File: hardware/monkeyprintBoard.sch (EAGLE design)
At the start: 46 parts, among them Q1 BSS123

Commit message: Updated eagle files.
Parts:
- removed GPIO: (no value), connectors:X05X2D
- removed H1, H2, H3, H4: MOUNT-HOLE3.0, holes:MOUNT-HOLE3.0
- removed U$2, U$3: POLOLU8825, pololu8825:POLOLU8825
- added ARDUINO_PRO_MICRO: ARDUINOPROMICRO, arduinoProMicro:ARDUINOPROMICRO
- added C7: 100n, rcl:C-EUC0603
- added POLOLU_DRV8825_BUILD, POLOLU_DRV8825_TILT: POLOLU8825, pololu8825:POLOLU8825
- added R15: 220R, rcl:R-EU_R0603
- added R17: 10k, rcl:R-EU_R0603
- added R19: 0R, rcl:R-EU_R0603
- added X3: (no value), connectors:X02
- U$1: value ARDUINOPROMICRO -> MONKEYPRINTPICONNECTOR; device arduinoProMicro:ARDUINOPROMICRO -> monkeyprintPiConnector:MONKEYPRINTPICONNECTOR
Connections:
- new net N$49: R17.1, R19.2, U$6.6
- new net N$50: ARDUINO_PRO_MICRO.(MOSI)PB2, C7.1, R19.1
- net GND: now also ARDUINO_PRO_MICRO.GND1, ARDUINO_PRO_MICRO.GND2, ARDUINO_PRO_MICRO.GND3, C7.2, POLOLU_DRV8825_BUILD.GND1, POLOLU_DRV8825_BUILD.GND2, POLOLU_DRV8825_TILT.GND1, POLOLU_DRV8825_TILT.GND2, X3.2; no longer GPIOA.9, GPIOB.6, U$1.GND3, U$2.GND1, U$2.GND2, U$3.GND1, U$3.GND2
- net N$1: now also ARDUINO_PRO_MICRO.PD4, POLOLU_DRV8825_BUILD.DIR; no longer U$1.PD4, U$2.DIR
- net N$12: now also ARDUINO_PRO_MICRO.PD1(INT1/SDA); no longer U$1.PD1(INT1/SDA)
- net N$13: now also ARDUINO_PRO_MICRO.PD0(INT0/SCL/OC0B); no longer U$1.PD0(INT0/SCL/OC0B)
- net N$15: now also POLOLU_DRV8825_BUILD.2A; no longer U$2.2A
- net N$16: now also POLOLU_DRV8825_BUILD.1A; no longer U$2.1A
- net N$17: now also POLOLU_DRV8825_BUILD.1B; no longer U$2.1B
- net N$18: now also POLOLU_DRV8825_TILT.2A; no longer U$3.2A
- net N$19: now also POLOLU_DRV8825_TILT.1A; no longer U$3.1A
- net N$2: now also ARDUINO_PRO_MICRO.PC6(OC3A), POLOLU_DRV8825_BUILD.STEP; no longer U$1.PC6(OC3A), U$2.STEP
- net N$20: now also POLOLU_DRV8825_TILT.1B; no longer U$3.1B
- net N$21: now also POLOLU_DRV8825_TILT.2B; no longer U$3.2B
- net N$22: now also POLOLU_DRV8825_TILT.M0; no longer U$3.M0
- net N$23: now also POLOLU_DRV8825_TILT.M1; no longer U$3.M1
- net N$24: now also POLOLU_DRV8825_TILT.M2; no longer U$3.M2
- net N$25: now also ARDUINO_PRO_MICRO.PE6(INT6); no longer U$1.PE6(INT6)
- net N$26: now also ARDUINO_PRO_MICRO.PD3(INT3/TXD), U$1.RXD; no longer GPIOB.10, U$1.PD3(INT3/TXD)
- net N$27: now also ARDUINO_PRO_MICRO.(OC1B)PB6; no longer U$1.(OC1B)PB6
- net N$28: now also ARDUINO_PRO_MICRO.RESET; no longer U$1.RESET
- net N$29: now also ARDUINO_PRO_MICRO.(SCK)PB1, U$7.4; no longer U$1.(SCK)PB1, U$7.1
- net N$31: now also X3.1; no longer U$7.4
- net N$32: now also ARDUINO_PRO_MICRO.PF5; no longer U$1.PF5
- net N$33: now also ARDUINO_PRO_MICRO.VCC; no longer U$1.VCC
- net N$34: now also ARDUINO_PRO_MICRO.PF4; no longer U$1.PF4
- net N$37: now also ARDUINO_PRO_MICRO.PD2(INT2/RXD), U$1.TXD; no longer GPIOB.8, U$1.PD2(INT2/RXD)
- net N$38: now also ARDUINO_PRO_MICRO.(MISO/LED)PB3, U$7.6; no longer U$1.(MISO/LED)PB3, U$7.3
- net N$39: now also ARDUINO_PRO_MICRO.PD7(OC4D), U$7.1; no longer U$1.PD7(OC4D), U$6.4
- net N$4: now also ARDUINO_PRO_MICRO.PB5(OC1A), POLOLU_DRV8825_TILT.STEP; no longer U$1.PB5(OC1A), U$3.STEP
- net N$41: now also R15.1, U$6.4; no longer U$1.(MOSI)PB2, U$7.6
- net N$42: now also POLOLU_DRV8825_BUILD.2B; no longer U$2.2B
- net N$43: now also POLOLU_DRV8825_BUILD.VMOTOR; no longer U$2.VMOTOR
- net N$44: now also POLOLU_DRV8825_BUILD.M0; no longer U$2.M0
- net N$45: now also POLOLU_DRV8825_BUILD.M1; no longer U$2.M1
- net N$46: now also POLOLU_DRV8825_BUILD.M2; no longer U$2.M2
- net N$5: now also ARDUINO_PRO_MICRO.PF6, POLOLU_DRV8825_BUILD.RESET, POLOLU_DRV8825_BUILD.SLEEP; no longer U$1.PF6, U$2.RESET, U$2.SLEEP
- net N$6: now also ARDUINO_PRO_MICRO.PB4, POLOLU_DRV8825_TILT.DIR; no longer U$1.PB4, U$3.DIR
- net N$8: now also ARDUINO_PRO_MICRO.PF7, POLOLU_DRV8825_TILT.RESET, POLOLU_DRV8825_TILT.SLEEP; no longer U$1.PF7, U$3.RESET, U$3.SLEEP
- net V+: now also POLOLU_DRV8825_TILT.VMOTOR; no longer U$3.VMOTOR
- net VCC: now also R15.2, R17.2, U$1.VCC1, U$1.VCC2, U$7.3; no longer GPIOB.2, GPIOB.4, U$6.6
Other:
- note added: "End stop tilt 2"
- note added: "LM2596"
- note added: "Raspberry Pi GPIO connector"
- note removed: "Camera trigger"
- moved on the sheet: C1, C2, C3, C4, C5, C6, D1, FAN, J1, J2, J3, J4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

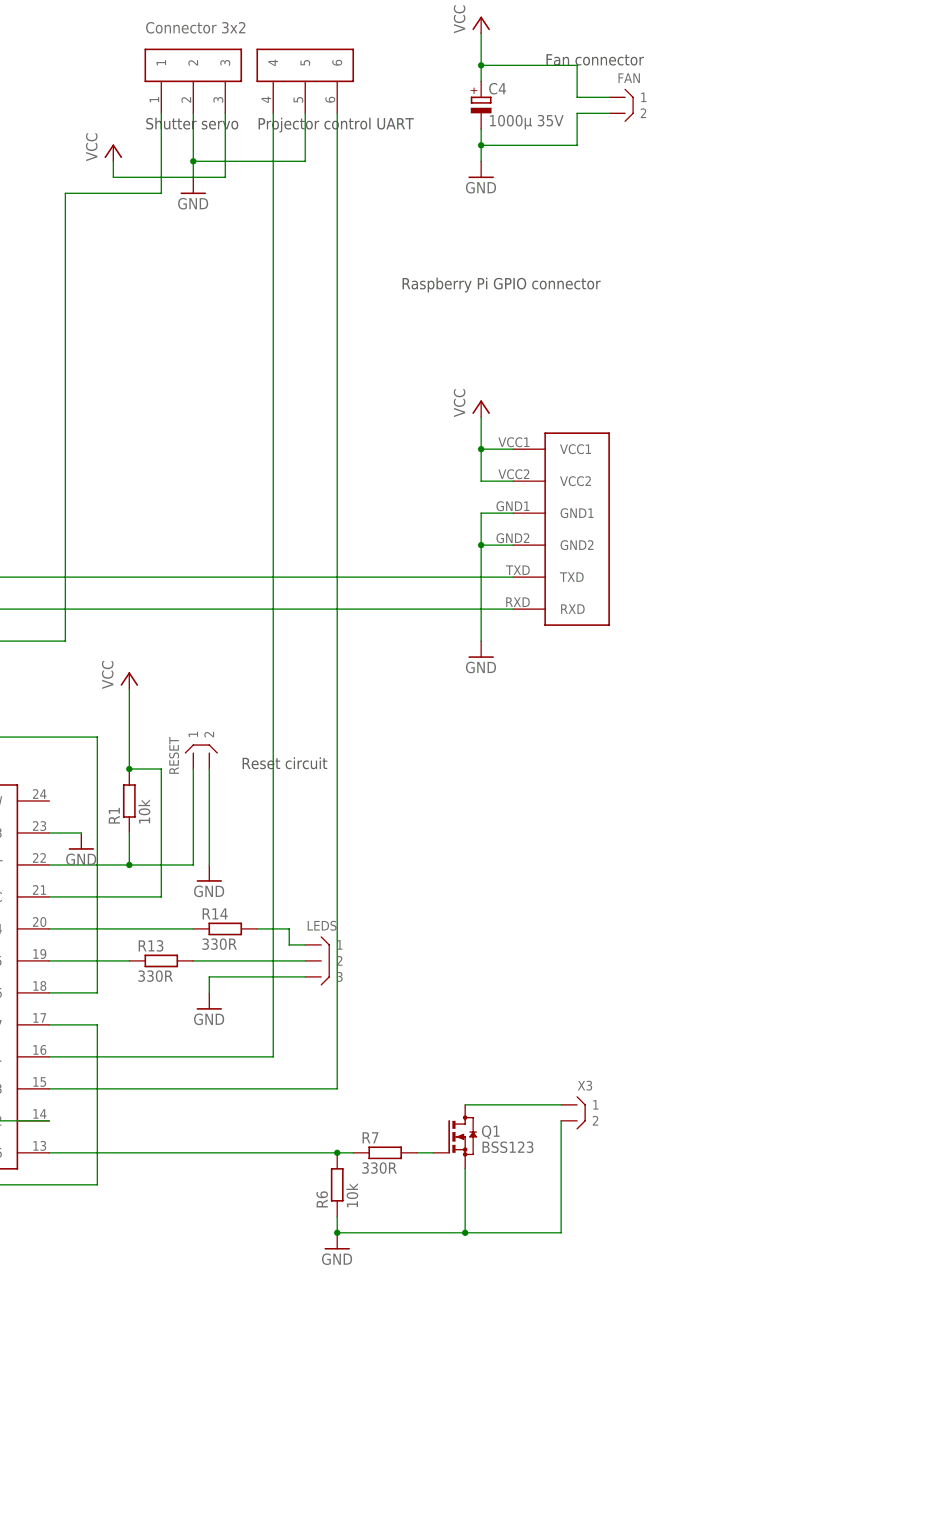
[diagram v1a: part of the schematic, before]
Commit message: Published board version 0.92. Fixed shutter servo pinout, swapped gnd and vcc to accomodate most common servo connector pinout.
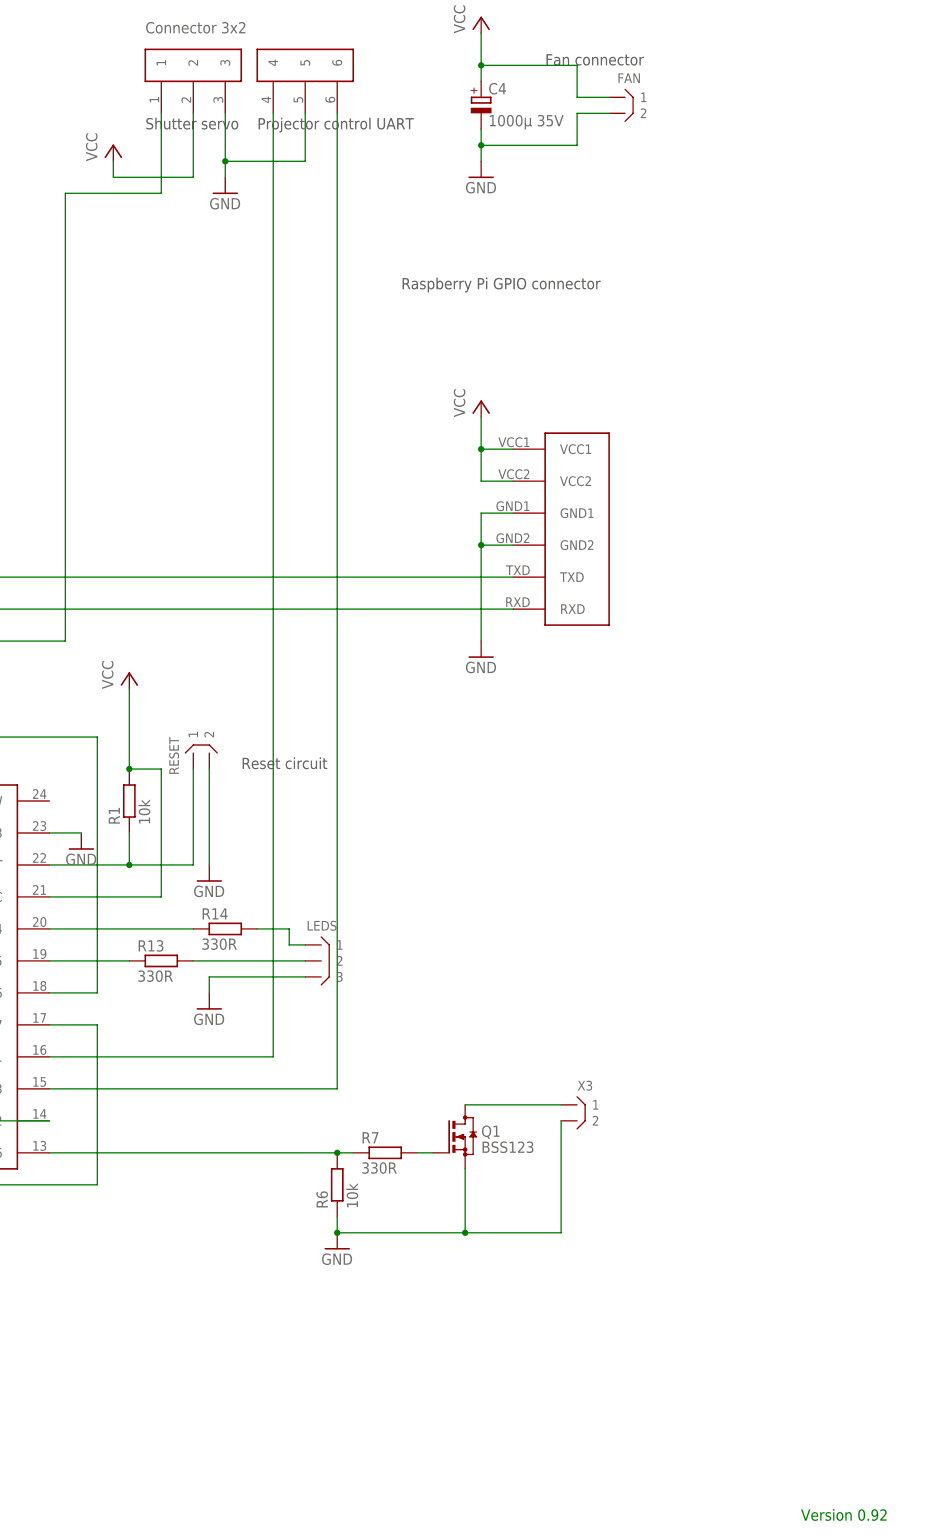
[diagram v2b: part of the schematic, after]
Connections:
- net GND: now also U$7.3; no longer U$7.2
- net VCC: now also U$7.2; no longer U$7.3
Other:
- note added: "Version 0.92"
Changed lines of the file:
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@@
 <text x="-152.4" y="104.14" size="1.778" layer="91">LM2596</text>
 <text x="76.2" y="106.68" size="1.778" layer="97">Raspberry Pi GPIO connector</text>
+<text x="139.7" y="-88.9" size="1.778" layer="91">Version 0.92</text>
 </plain>
 <instances>
@@
 <instance part="GND10" gate="1" x="66.04" y="-45.72"/>
 <instance part="Q1" gate="G$1" x="86.36" y="-27.94"/>
-<instance part="GND11" gate="1" x="43.18" y="121.92"/>
+<instance part="GND11" gate="1" x="48.26" y="121.92"/>
 <instance part="GND12" gate="1" x="-50.8" y="121.92"/>
 <instance part="P+9" gate="VCC" x="30.48" y="129.54"/>
@@
 </segment>
 <segment>
-<pinref part="U$7" gate="G$1" pin="2"/>
 <pinref part="GND11" gate="1" pin="GND"/>
-<wire x1="43.18" y1="134.62" x2="43.18" y2="127" width="0.1524" layer="91"/>
 <pinref part="U$7" gate="G$1" pin="5"/>
-<wire x1="43.18" y1="127" x2="43.18" y2="124.46" width="0.1524" layer="91"/>
+<wire x1="48.26" y1="127" x2="48.26" y2="124.46" width="0.1524" layer="91"/>
 <wire x1="60.96" y1="134.62" x2="60.96" y2="127" width="0.1524" layer="91"/>
-<wire x1="60.96" y1="127" x2="43.18" y2="127" width="0.1524" layer="91"/>
-<junction x="43.18" y="127"/>
+<wire x1="60.96" y1="127" x2="48.26" y2="127" width="0.1524" layer="91"/>
+<pinref part="U$7" gate="G$1" pin="3"/>
+<wire x1="48.26" y1="134.62" x2="48.26" y2="127" width="0.1524" layer="91"/>
+<junction x="48.26" y="127"/>
 </segment>
 <segment>
@@
 </segment>
 <segment>
-<wire x1="48.26" y1="124.46" x2="30.48" y2="124.46" width="0.1524" layer="91"/>
+<wire x1="43.18" y1="124.46" x2="30.48" y2="124.46" width="0.1524" layer="91"/>
 <wire x1="30.48" y1="124.46" x2="30.48" y2="127" width="0.1524" layer="91"/>
 <pinref part="P+9" gate="VCC" pin="VCC"/>
-<pinref part="U$7" gate="G$1" pin="3"/>
-<wire x1="48.26" y1="124.46" x2="48.26" y2="134.62" width="0.1524" layer="91"/>
-</segment>
-<segment>
+<pinref part="U$7" gate="G$1" pin="2"/>
+<wire x1="43.18" y1="124.46" x2="43.18" y2="134.62" width="0.1524" layer="91"/>
+</segment>
+<segment>
